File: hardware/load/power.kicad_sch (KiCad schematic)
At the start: 9 parts, among them Q501 2STC4468, Q503 2STC4468, U501 LTSR25-NP

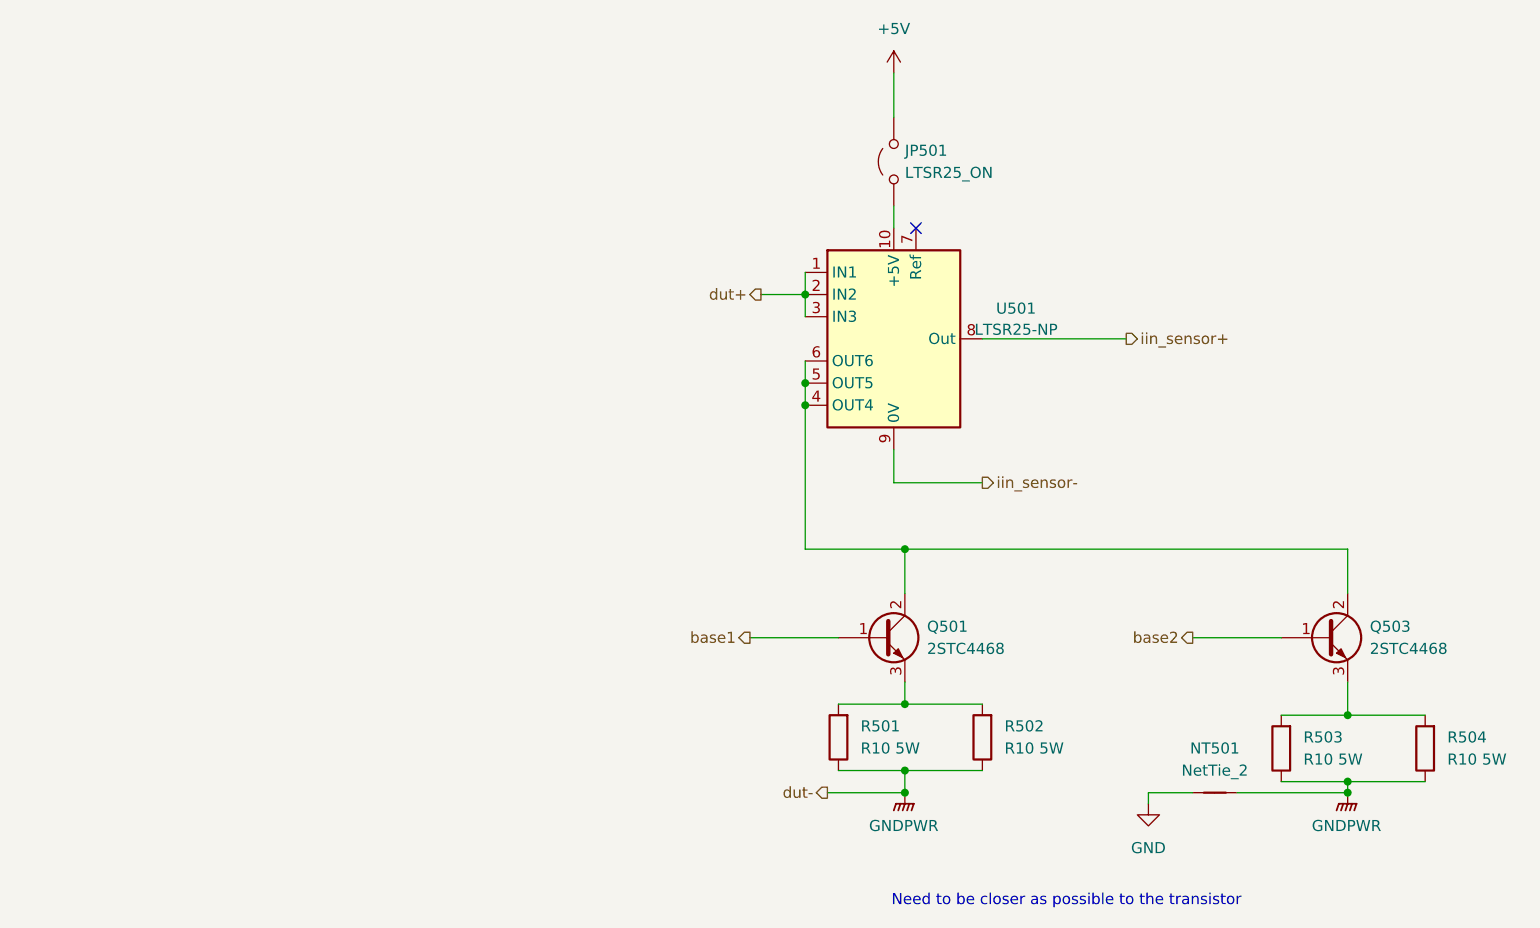
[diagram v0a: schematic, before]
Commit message: feat(load): route logic and optmize layout
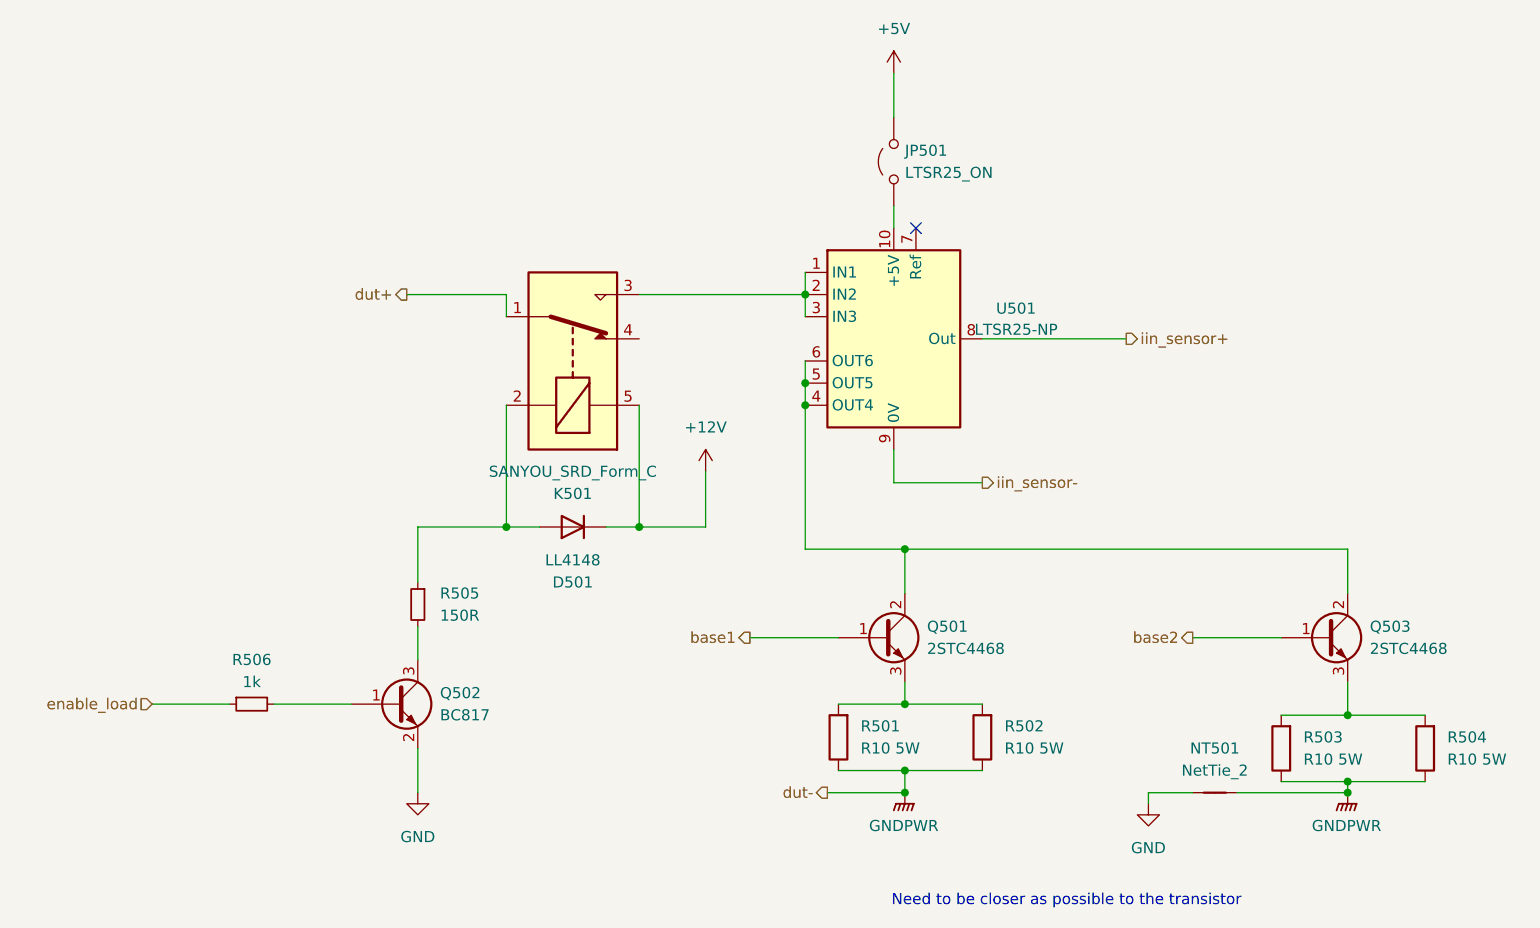
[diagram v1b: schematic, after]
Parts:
- added D501: LL4148, Diode_SMD:D_MiniMELF, symbol Diode:LL4148
- added K501: SANYOU_SRD_Form_C, Relay_THT:Relay_SPDT_SANYOU_SRD_Series_Form_C, symbol Relay:SANYOU_SRD_Form_C
- added Q502: BC817, Package_TO_SOT_SMD:SOT-23, symbol Transistor_BJT:BC817
- added R505: 150R, Resistor_SMD:R_0805_2012Metric_Pad1.20x1.40mm_HandSolder, symbol Device:R_Small
- added R506: 1k, Resistor_SMD:R_0805_2012Metric_Pad1.20x1.40mm_HandSolder, symbol Device:R_Small
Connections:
- net GND: now also Q502.2 (E)
- net dut+: now also K501.1; no longer U501.1 (IN1), U501.2 (IN2), U501.3 (IN3)
- new net: D501.2 (A), K501.2, R505.1
- new net: K501.3, U501.1 (IN1), U501.2 (IN2), U501.3 (IN3)
- new net: Q502.1 (B), R506.2
- new net: Q502.3 (C), R505.2
- new net +12V: D501.1 (K), K501.5
- new net enable_load: R506.1

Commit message: feat(load): fix DRC errors and warinigs
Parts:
- removed Q501, Q503: 2STC4468, TerminalBlock:TerminalBlock_bornier-3_P5.08mm, symbol Device:Q_NPN_BCE
- added Q501, Q504: 2STC4468, TerminalBlock:TerminalBlock_bornier-3_P5.08mm, symbol Device:Q_NPN_ECB
- JP501: footprint Jumper:SolderJumper-2_P1.3mm_Open_TrianglePad1.0x1.5mm -> Load:SolderJumper-2_P1.3mm_Open_TrianglePad1.0x1.5mm
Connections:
- net base1: now also Q504.3 (B)
- net base2: now also Q501.3 (B)
- net at U501.4 (OUT4), U501.5 (OUT5), U501.6 (OUT6): now also Q501.2 (C), Q504.2 (C)
- net at R501.2, R502.2: now also Q504.1 (E)
- net at R503.2, R504.2: now also Q501.1 (E)
